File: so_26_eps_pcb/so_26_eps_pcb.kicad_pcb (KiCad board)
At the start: 4 copper layers, 90.2 x 95.9 mm, 48 parts, among them J1 Conn_02x12_Odd_Even, J2 Conn_01x02, J3 Conn_01x02, SW1 SW_SPDT

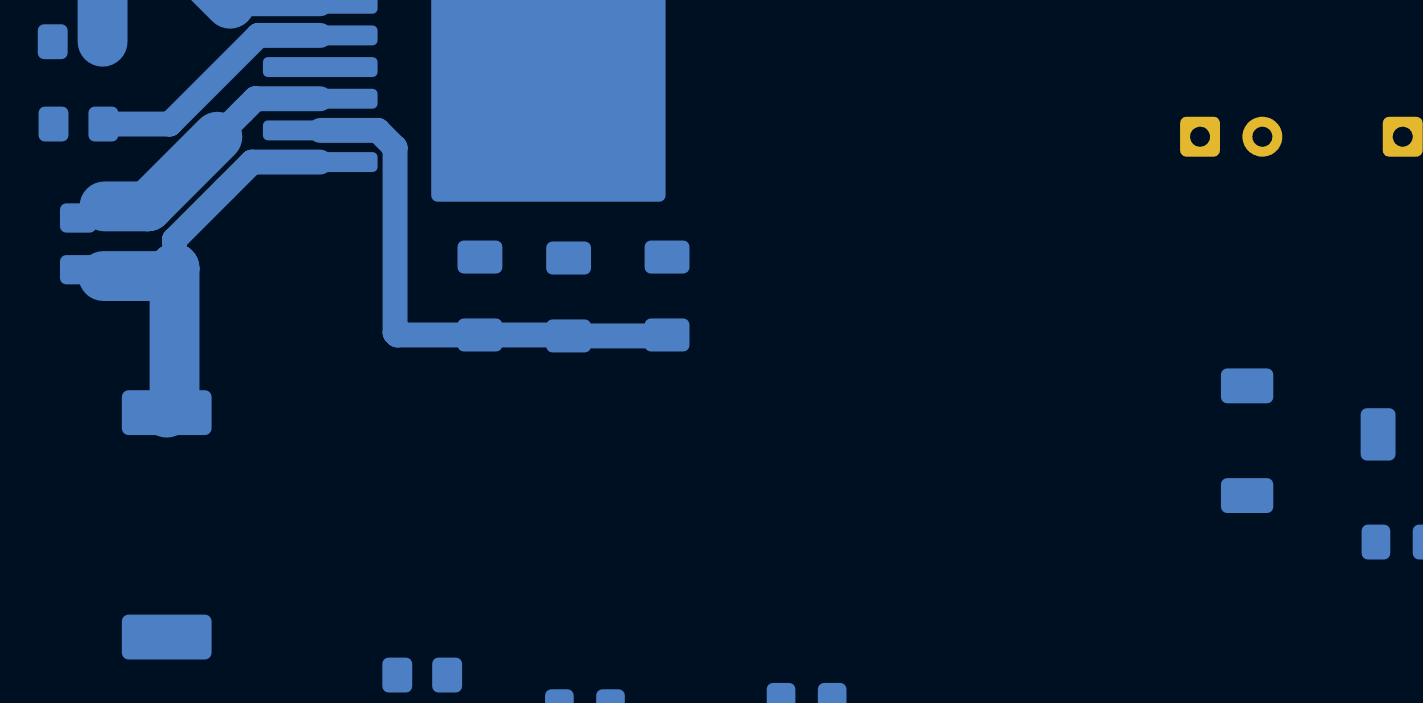
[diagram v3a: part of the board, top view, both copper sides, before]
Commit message: Finished rooting the positive parts
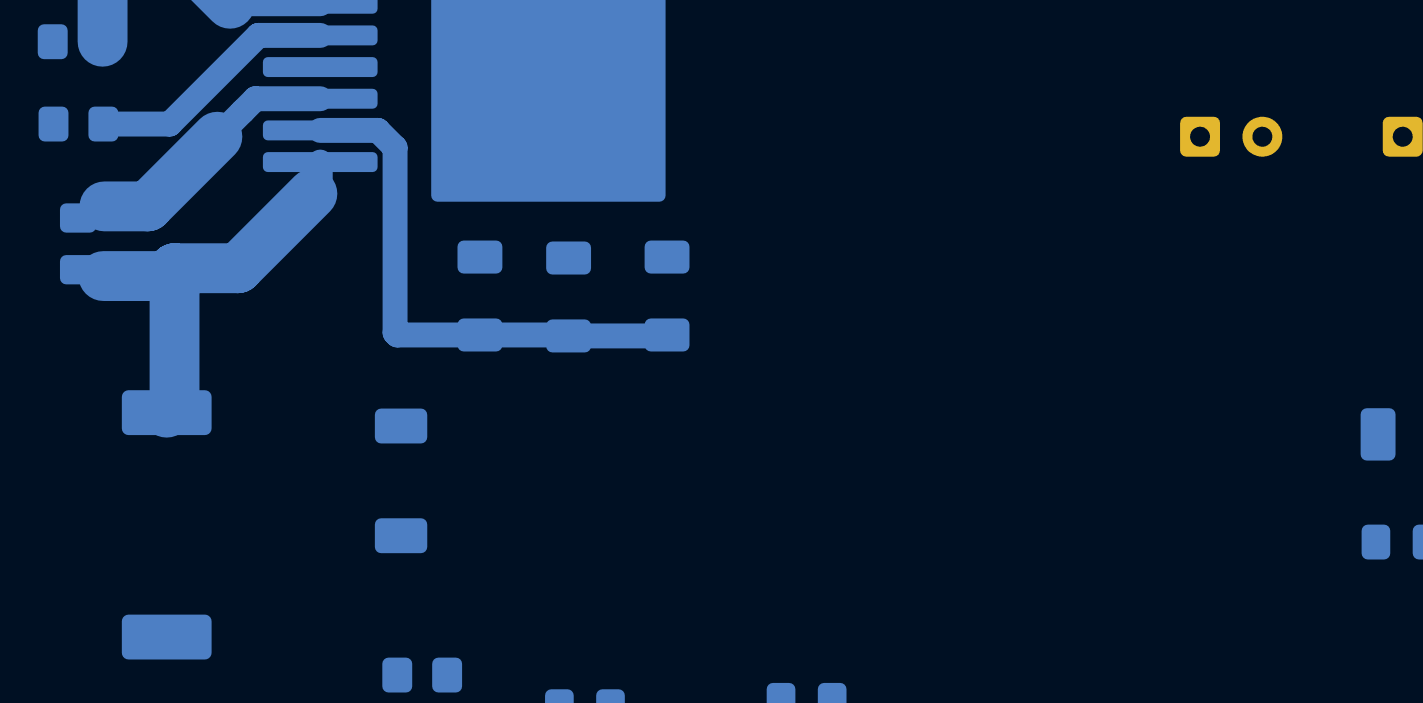
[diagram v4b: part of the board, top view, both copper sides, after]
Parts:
- moved D1 34.0 mm to (85.9, 60.6)
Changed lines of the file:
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@@
 	(footprint "Diode_SMD:D_SOD-128"
 		(layer "B.Cu")
-		(at 119.784 58.997 -90)
+		(at 85.852 60.607 -90)
 		(descr "D_SOD-128 (CFP5 SlimSMAW), https://assets.nexperia.com/documents/outline-drawing/SOD128.pdf")
 		(tags "D_SOD-128")
@@
 	)
 	(segment
-		(start 82.611 47.82175)
-		(end 79.874828 47.82175)
+		(start 82.611 48.776)
+		(end 82.296 49.091)
 		(width 1)
 		(layer "B.Cu")
@@
 	)
 	(segment
-		(start 76.767789 52.079211)
-		(end 76.454 52.393)
+		(start 79.307789 52.079211)
+		(end 76.767789 52.079211)
 		(width 2)
 		(layer "B.Cu")
@@
 	)
 	(segment
-		(start 79.874828 47.82175)
-		(end 78.799789 48.896789)
-		(width 1)
+		(start 82.296 49.091)
+		(end 79.307789 52.079211)
+		(width 2)
 		(layer "B.Cu")
 		(net 6)
@@
 	(segment
 		(start 76.767789 52.079211)
-		(end 76.767789 57.557211)
+		(end 76.454 52.393)
 		(width 2)
 		(layer "B.Cu")
@@
 	)
 	(segment
-		(start 76.767789 50.928789)
-		(end 76.767789 52.079211)
+		(start 82.611 47.82175)
+		(end 82.611 48.776)
 		(width 1)
 		(layer "B.Cu")
@@
 	)
 	(segment
-		(start 78.799789 48.896789)
-		(end 76.767789 50.928789)
-		(width 1)
+		(start 76.767789 52.079211)
+		(end 76.767789 57.557211)
+		(width 2)
 		(layer "B.Cu")
 		(net 6)

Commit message: Saved
some changes needs to be done on the wires
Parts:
- removed J2: Conn_01x02, Myfootprints:01x02_header
- moved JP1 74.1 mm to (127.0, 36.1)
- moved R5 73.4 mm to (138.7, 75.5), turned to -90 degrees
- moved L2 67.3 mm to (83.9, 47.7), turned to 90 degrees
- moved C17 64.9 mm to (145.0, 99.6)
- moved L1 63.2 mm to (130.4, 82.2), turned to 0 degrees
- moved R9 58.7 mm to (86.1, 43.8), turned to -90 degrees
- moved C15 58.0 mm to (145.0, 95.3)
- moved R11 57.8 mm to (144.5, 68.1), turned to 90 degrees
- moved R2 54.1 mm to (116.8, 48.1), turned to 180 degrees
- moved R1 53.4 mm to (116.6, 51.6)
- moved C9 51.6 mm to (120.9, 69.9), turned to 180 degrees
- moved R10 49.4 mm to (93.2, 43.8), turned to -90 degrees
- moved R7 49.1 mm to (119.6, 54.4), turned to 90 degrees
- moved C18 46.6 mm to (74.0, 72.7)
- moved C11 44.6 mm to (136.8, 87.2), turned to 180 degrees
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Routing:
- net +3V3: track 0.00 -> 95.9 mm
- net Net-(CELL_1-Pad6): track 0.00 -> 86.3 mm
- net REG_+10V: track 0.00 -> 82.9 mm
- net Net-(CELL_1-Pad2): track 0.00 -> 80.9 mm
- net Net-(CELL_1-Pad4): track 0.00 -> 80.9 mm
- net Net-(J3-Pin_1): track 0.00 -> 64.7 mm
- net REG_+3V3: track 0.00 -> 44.1 mm
- net Net-(10V_Regulator1-SW): track 0.00 -> 35.2 mm
- net Net-(3V3_Regulator1-FB): track 13.2 -> 48.4 mm
- net Net-(SW1-B): track 0.00 -> 32.6 mm
- net +10V_ALT: track 0.00 -> 29.9 mm
- net +10V: track 0.00 -> 26.5 mm
- net /VBAT_1: track 0.00 -> 21.1 mm
- net Net-(JP1-C): track 0.00 -> 20.1 mm, vias 0 -> 2
- net /VBAT_0: track 0.00 -> 19.2 mm
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- added copper zone on B.Cu, net VBAT

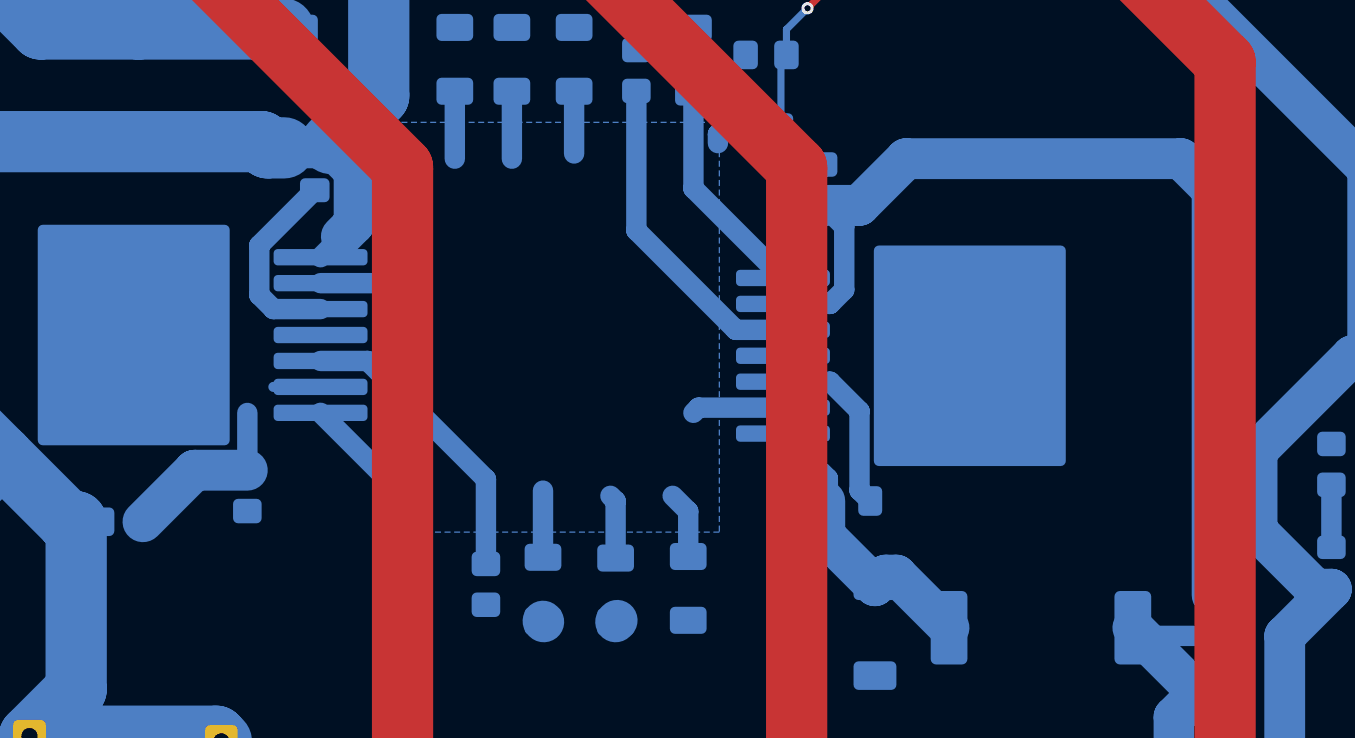
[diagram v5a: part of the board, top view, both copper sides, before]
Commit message: Changed the thickness on some wires
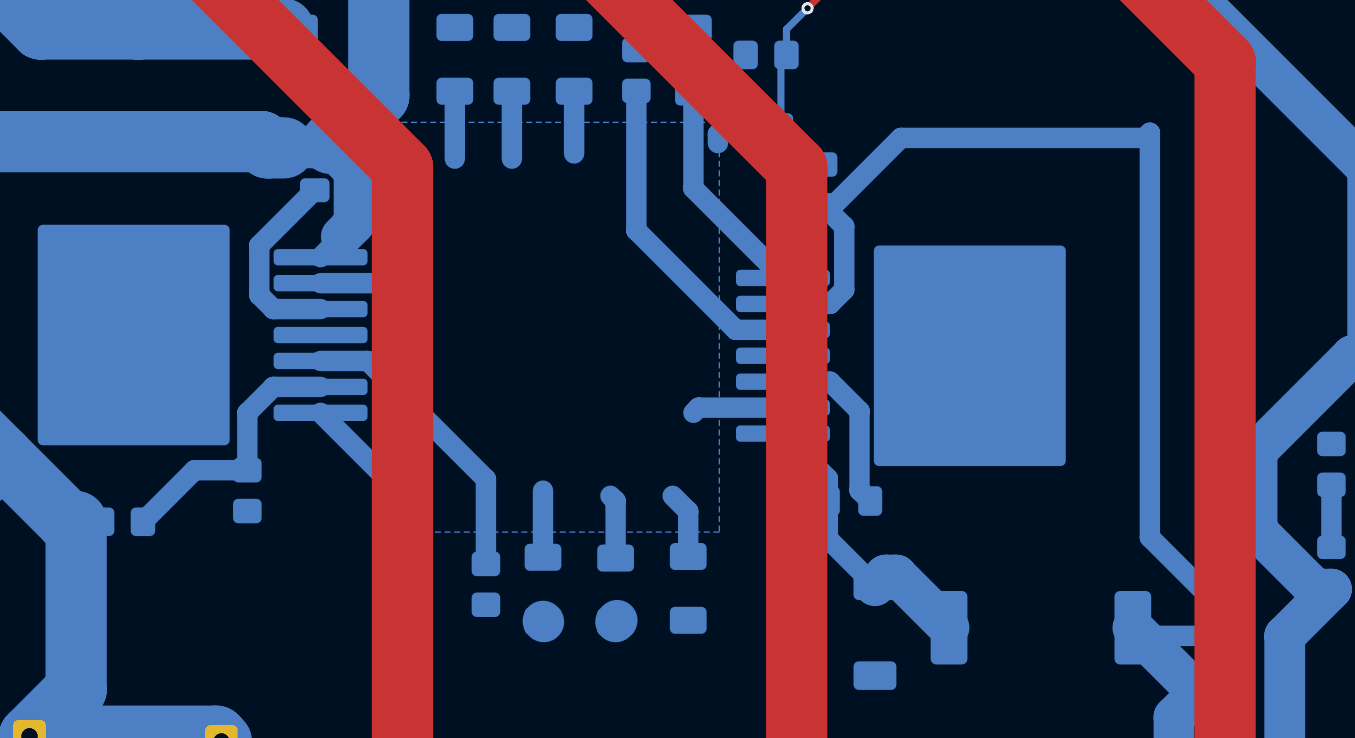
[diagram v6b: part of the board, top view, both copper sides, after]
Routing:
- net Net-(10V_Regulator1-FB): track 11.5 -> 13.3 mm
- net Net-(3V3_Regulator1-FB): track 48.4 -> 49.4 mm
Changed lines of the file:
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@@
-	)
-	(segment
-		(start 123.698 53.155)
-		(end 121.412 55.441)
-		(width 2)
-		(layer "B.Cu")
-		(net 3)
-	)
-	(segment
-		(start 121.412 55.441)
-		(end 119.634 55.441)
-		(width 2)
-		(layer "B.Cu")
-		(net 3)
 	)
 	(segment
@@
 	)
 	(segment
+		(start 135.382 52.139)
+		(end 135.636 51.885)
+		(width 1)
+		(layer "B.Cu")
+		(net 3)
+	)
+	(segment
+		(start 123.444 52.139)
+		(end 135.382 52.139)
+		(width 1)
+		(layer "B.Cu")
+		(net 3)
+	)
+	(segment
+		(start 120.142 55.441)
+		(end 123.444 52.139)
+		(width 1)
+		(layer "B.Cu")
+		(net 3)
+	)
+	(segment
 		(start 120.67 59.575748)
 		(end 120.67 56.477)
@@
 	)
 	(segment
+		(start 119.634 55.441)
+		(end 120.142 55.441)
+		(width 1)
+		(layer "B.Cu")
+		(net 3)
+	)
+	(segment
+		(start 138.462 74.523)
+		(end 138.684 74.523)
+		(width 1)
+		(layer "B.Cu")
+		(net 3)
+	)
+	(segment
 		(start 120.67 56.477)
 		(end 119.634 55.441)
@@
 	)
 	(segment
-		(start 138.684 54.679)
-		(end 137.16 53.155)
-		(width 2)
-		(layer "B.Cu")
-		(net 3)
-	)
-	(segment
-		(start 138.684 74.523)
-		(end 138.684 54.679)
-		(width 2)
-		(layer "B.Cu")
-		(net 3)
-	)
-	(segment
-		(start 137.16 53.155)
-		(end 123.698 53.155)
-		(width 2)
+		(start 135.636 51.885)
+		(end 135.636 71.697)
+		(width 1)
 		(layer "B.Cu")
 		(net 3)
@@
 	)
 	(segment
+		(start 135.636 71.697)
+		(end 138.462 74.523)
+		(width 1)
+		(layer "B.Cu")
+		(net 3)
+	)
+	(segment
 		(start 115.359252 61.537)
 		(end 117.669 61.537)
@@
 	)
 	(segment
+		(start 119.8665 71.7615)
+		(end 122.174 74.069)
+		(width 1)
+		(layer "B.Cu")
+		(net 6)
+	)
+	(segment
 		(start 122.696 73.547)
 		(end 122.174 74.069)
@@
 	)
 	(segment
-		(start 119.717 71.612)
-		(end 119.717 69.919)
-		(width 2)
-		(layer "B.Cu")
-		(net 6)
-	)
-	(segment
-		(start 122.174 74.069)
-		(end 119.717 71.612)
-		(width 2)
-		(layer "B.Cu")
-		(net 6)
-	)
-	(segment
 		(start 119.8665 68.8145)
 		(end 117.669 66.617)
@@
 		(start 119.8665 69.919)
 		(end 119.8665 68.8145)
+		(width 1)
+		(layer "B.Cu")
+		(net 6)
+	)
+	(segment
+		(start 119.8665 69.919)
+		(end 119.8665 71.7615)
 		(width 1)
 		(layer "B.Cu")
@@
 		(start 91.44 68.411)
 		(end 88.852 68.411)
-		(width 2)
+		(width 1)
 		(layer "B.Cu")
 		(net 21)
@@
 	)
 	(segment
+		(start 95.026 64.331)
+		(end 92.716252 64.331)
+		(width 1)
+		(layer "B.Cu")
+		(net 21)
+	)
+	(segment
 		(start 88.852 68.411)
 		(end 86.328 70.935)
-		(width 2)
+		(width 1)
+		(layer "B.Cu")
+		(net 21)
+	)
+	(segment
+		(start 92.716252 64.331)
+		(end 91.44 65.607252)
+		(width 1)
 		(layer "B.Cu")
 		(net 21)
@@
 		(layer "B.Cu")
 		(net 21)
-	)
-	(segment
-		(start 95.026 64.331)
-		(end 92.716252 64.331)
-		(width 0.5)
-		(layer "B.Cu")
-		(net 21)

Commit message: REV 1 FINAL
SHEMATIC AND PCB CHECK
DRC/ERC PASSED
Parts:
- 18650 BATTERY HOLDER: renamed from CELL_1
- moved R11 82.7 mm to (70.9, 105.8), turned to 0 degrees
- moved D4 79.7 mm to (70.9, 103.6), turned to 0 degrees
- moved D6 64.2 mm to (70.9, 94.0), turned to 0 degrees
- moved R13 61.5 mm to (70.8, 96.5), turned to 0 degrees
- moved D3 50.1 mm to (118.5, 43.9)
- moved J3 48.4 mm to (81.6, 120.9), turned to 180 degrees
- moved R12 47.8 mm to (70.8, 86.2), turned to 0 degrees
- moved C17 46.2 mm to (135.7, 54.4)
- moved D5 46.1 mm to (70.9, 84.0), turned to 0 degrees
- moved C15 41.9 mm to (129.1, 56.6), turned to 0 degrees
- moved C11 37.1 mm to (123.4, 52.6)
- moved C13 36.8 mm to (129.4, 50.4), turned to -90 degrees
- moved C16 33.8 mm to (99.2, 54.5), turned to 180 degrees
- moved D2 33.6 mm to (82.0, 71.1), turned to -90 degrees
- moved C3 32.1 mm to (123.2, 74.3), turned to 180 degrees
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- renumbered 3V3_Regulator1 to U1, 10V_Regulator1 to U2
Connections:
- D5 pad 1: +10V -> Net-(D5-K)
- D6 pad 1: +10V_ALT -> Net-(D6-K)
- R12 pad 1: +10V -> Net-(D5-K)
- R13 pad 1: +10V_ALT -> Net-(D6-K)
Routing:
- net REG_+10V: track 82.9 -> 0.00 mm
- net VBAT: track 29.8 -> 110.6 mm, vias 0 -> 17
- net GND: track 0.35 -> 53.9 mm, vias 0 -> 142
- net Net-(J3-Pin_1): track 64.7 -> 14.7 mm
- net REG_+3V3: track 44.1 -> 0.00 mm
- net +10V_ALT: track 29.9 -> 73.1 mm, vias 0 -> 1
- net Net-(3V3_Regulator1-FB): track 49.4 -> 8.32 mm
- net Net-(10V_Regulator1-SW): track 35.2 -> 0.00 mm
- net +10V: track 26.5 -> 54.9 mm
- net Net-(3V3_Regulator1-SW): track 14.2 -> 0.00 mm
- net Net-(3V3_Regulator1-IADJ): track 16.0 -> 4.26 mm
- net Net-(10V_Regulator1-IADJ): track 14.6 -> 4.26 mm
- net Net-(JP1-C): track 20.1 -> 9.90 mm, vias 2 -> 0
- net Net-(3V3_Regulator1-SS): track 10.9 -> 2.98 mm
- net +3V3: track 95.9 -> 103.5 mm, vias 0 -> 2
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- added copper zone on B.Cu, net +10V
- added copper zone on B.Cu, net +10V_ALT
- added copper zone on B.Cu, net +3V3
- added copper zone on B.Cu, net GND
- added copper zone on F.Cu, net GND
- added copper zone on B.Cu, net Net-(10V_Regulator1-SW)
- added copper zone on B.Cu, net Net-(3V3_Regulator1-SW)
- added copper zone on B.Cu, net REG_+10V
- added copper zone on B.Cu, net REG_+3V3
- added copper zone on F.Cu, net VBAT
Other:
- board text added: "+10V"
- board text added: "+3V3"
- board text added: "ALT_+10V"
- board text added: "SO26 - EPS KATHARINA NILSSEN 11.02.26"
- board text added: "VBAT_0"
- board text added: "VBAT_1"

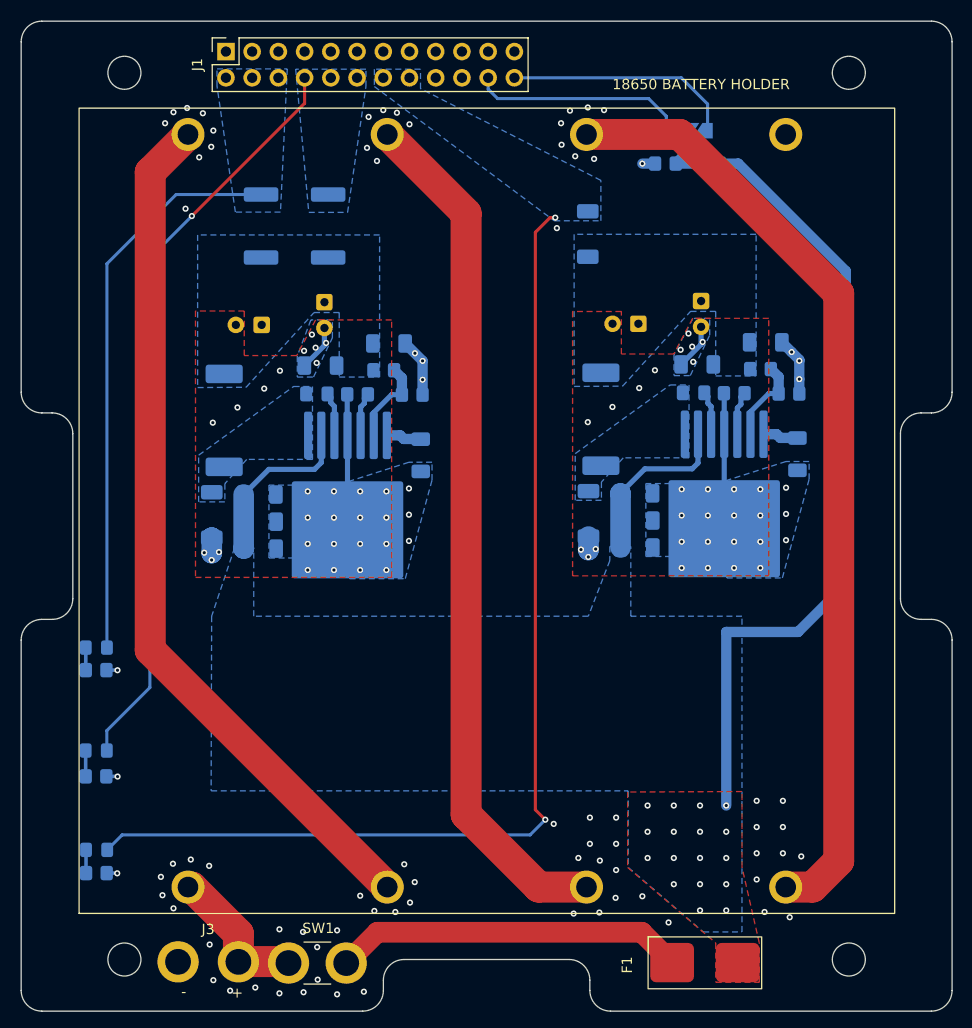
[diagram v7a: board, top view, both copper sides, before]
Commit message: added via stiching
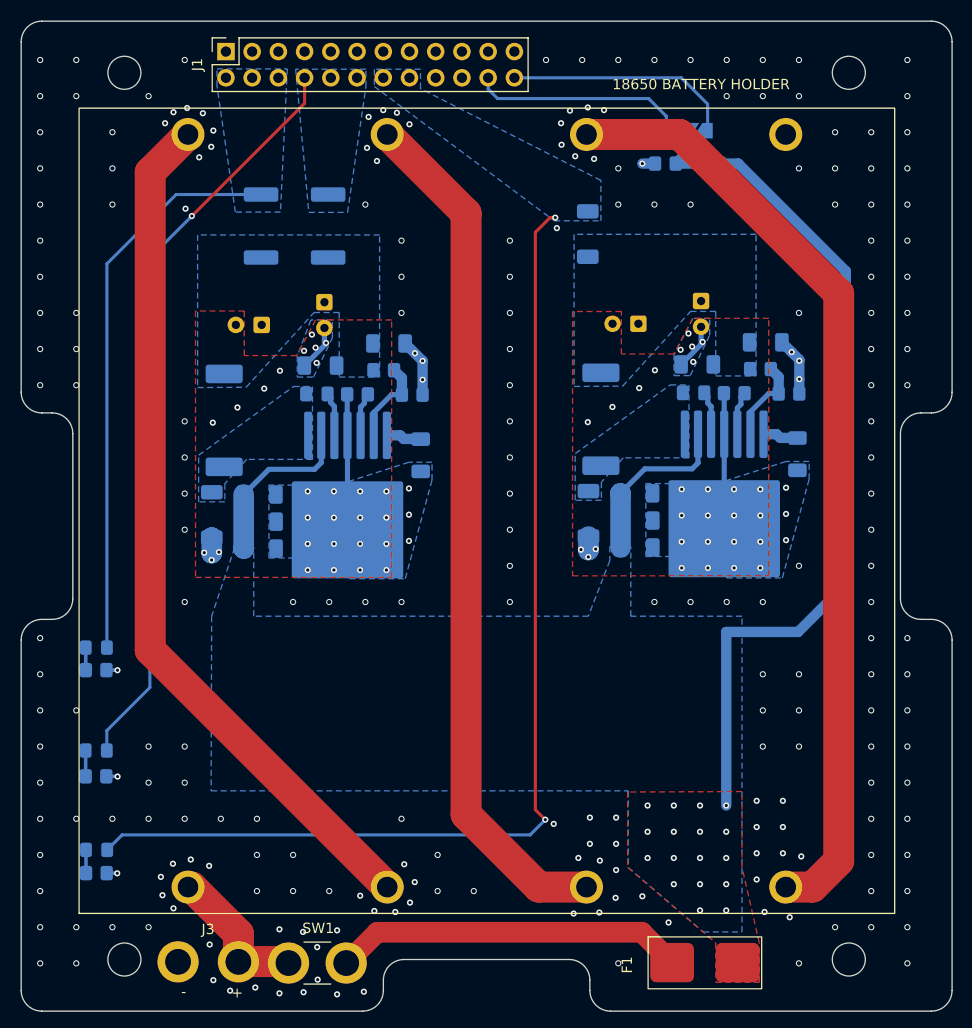
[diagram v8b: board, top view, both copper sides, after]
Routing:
- net GND: vias 142 -> 297
